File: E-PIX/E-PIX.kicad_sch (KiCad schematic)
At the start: 45 parts, among them J1 USB_C_Receptacle_USB2.0, J2 BNO055, J3 ADC, J4 ADC, Q1 BSS138, Q2 BSS138, SW1 SW, SW2 SW_Push, U1 Conn_03x04, U2 Conn_03x04, U3 TC7WH241FK, U4 TC7WH241FK, U5 NJM7805SDL1, U6 AZ1117-3.3, U7 ESP32-C3-WROOM-02, U8 BTS6142D

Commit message: add SD card mod
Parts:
- removed C6: 1u/16V, Capacitor_SMD:C_0603_1608Metric, symbol Device:C_Small
- removed D3: GREEN, LED_SMD:LED_0603_1608Metric, symbol Device:LED_Small
- removed J3, J4: ADC, Connector_PinHeader_2.54mm:PinHeader_1x03_P2.54mm_Vertical, symbol Connector_Generic:Conn_01x03
- removed R11: 510, Resistor_SMD:R_0603_1608Metric, symbol Device:R_Small
- removed R4, R7, R8: 10k, Resistor_SMD:R_0603_1608Metric, symbol Device:R_Small
- removed SW1: SW, Connector_PinHeader_2.54mm:PinHeader_1x02_P2.54mm_Vertical, symbol Switch:SW_DPST_x2
- removed U7: ESP32-C3-WROOM-02, Espressif:ESP32-C3-WROOM-02, symbol Espressif:ESP32-C3-WROOM-02
- removed U9: ~, IMU:BNO055, symbol IMU:BNO055
- added C6, C9: 47p, symbol Device:C
- added D4: WS2812B, LED_SMD:LED_WS2812B_PLCC4_5.0x5.0mm_P3.2mm, symbol LED:WS2812B
- added Q3, Q4: 2SC4213, Package_TO_SOT_SMD:SOT-323_SC-70, symbol Transistor_BJT:2SC4213
- added R11, R8: 47k, symbol Device:R
- added R15, R16: 470k, symbol Device:R
- added R4, R7: 27, symbol Device:R
- added U10: ESP32-S3-WROOM-1, RF_Module:ESP32-S3-WROOM-1, symbol RF_Module:ESP32-S3-WROOM-1
- added U7: FT231XS, Package_SO:SSOP-20_3.9x8.7mm_P0.635mm, symbol Interface_USB:FT231XS
- C8: value 0.1u/25V -> 0.2u/25V
- J2: footprint Connector_PinHeader_2.54mm:PinHeader_1x05_P2.54mm_Vertical -> Connector_JST:JST_XH_B4B-XH-A_1x04_P2.50mm_Vertical
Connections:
- net ADC1 is gone; now on net +3V3: R1.2
- net +3V3: now also U10.2 (3V3), U7.13 (3V3OUT), U7.3 (VCCIO); no longer C5.1
- net +5V: now also U7.15 (VCC); no longer C2.2
- net BNO055RST: now also U10.18 (IO10)
- net D+: now also R7.2
- net D-: now also R4.1
- net EN1: now also U10.4 (IO4)
- net EN2: now also U10.5 (IO5)
- net GND: now also J1.S1 (SHIELD), C6.1, C9.1, R15.1, R16.1, U10.1 (GND), U10.40 (GND), U10.41 (GND), U7.16 (GND), U7.6 (GND); no longer C2.1, C5.2, R1.1
- net RX1: now also U10.11 (IO18)
- net RX2: now also U10.22 (IO14)
- net SCL: now also U10.17 (IO9)
- net SDA: now also U10.12 (IO8)
- net TX1: now also U10.10 (IO17)
- net TX2: now also U10.21 (IO13)
- net at R9.1: now also U8.2 (IN)
- net at R9.2: no longer U8.2 (IN)
- net RST renamed EN
- net EN: now also R1.1, Q3.3 (C), U10.3 (EN)
- new net: C9.2, R7.1, U7.11 (USBDP)
- new net: Q3.1 (B), R8.1
- new net: C6.2, R4.2, U7.12 (USBDM)
- new net: Q4.1 (B), R11.1
- new net BOOT: Q4.3 (C), U10.27 (IO0)
- new net DTR: Q4.2 (E), R16.2, R8.2, U7.1 (~{DTR})
- new net RTS: Q3.2 (E), R11.2, R15.2, U7.2 (~{RTS})
- new net RX0: U10.36 (RXD0), U7.20 (TXD)
- new net TX0: U10.37 (TXD0), U7.4 (RXD)
- no-connect marks 5 -> 13
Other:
- note added: "Auto boot / Reset"
- note added: "DCDC 7.4V → 3.3V 1.35A"
- note added: "Protection"
- note added: "USB port"
- note added: "USB-Serial convertion"
- note removed: "BNO055"
- note removed: "CPU"
- note removed: "DCDC 5V → 3.3V 1.35A"
- note removed: "Load Switch"
- note removed: "Power supply 5V"
- note removed: "逆流防止用SBD 電圧降下のため デバックにしか使わない"
- moved on the sheet: C1, C2, C3, C4, C5, C7, C8, D1, D2, H1, H2, J1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

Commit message: complete main function. start checking
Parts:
- removed J2: BNO055, Connector_JST:JST_XH_B4B-XH-A_1x04_P2.50mm_Vertical, symbol Connector_Generic:Conn_01x05
- added D3: LED, symbol Device:LED
- added J3: DM3AT-SF-PEJM5, Connector_Card:microSD_HC_Hirose_DM3AT-SF-PEJM5, symbol DM3AT-SF-PEJM5:DM3AT-SF-PEJM5
- added R14: 100, symbol Device:R
- added U9: ~, IMU:BNO055, symbol IMU:BNO055
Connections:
- net +3V3: now also C3.2, C7.2, D4.1 (VDD), D3.2 (A), J3.4 (VDD), U9.1 (VIN); no longer C3.1, C7.1
- net BNO055RST: now also U10.7 (IO7), U9.5 (RESET); no longer U10.18 (IO10)
- net GND: now also C3.1, C7.1, D4.3 (VSS), J3.6 (VSS), J3.P1 (SHIELD), J3.P2 (SHIELD), J3.P3 (SHIELD), J3.P4 (SHIELD), R14.2, U9.2 (GND), U9.7 (GND); no longer C3.2, C7.2
- net RX2: now also U10.14 (IO20); no longer U10.22 (IO14)
- net SCL: now also U9.4 (SCL/R)
- net SDA: now also U9.3 (SDA/T)
- net TX2: now also U10.13 (IO19); no longer U10.21 (IO13)
- net MOSI: now reaches U10.19 (IO11)
- net MOSI: now also J3.3 (CMD)
- net CLK: now reaches U10.20 (IO12)
- net CLK: now also J3.5 (CLK)
- net RGB_led: now reaches U10.25 (IO48)
- net RGB_led: now also D4.4 (DIN)
- new net: D3.1 (K), R14.1
- new net CS: J3.2 (CD/DAT3), U10.18 (IO10)
- new net MISO: J3.7 (DAT0), U10.21 (IO13)
- no-connect marks 13 -> 17
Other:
- note added: "IO"
- note added: "SD card reader"
- note removed: "Output"
- moved on the sheet: C3, C7, D4, H3, H4, Q1, Q2, R12, R13, R5, R6, U1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

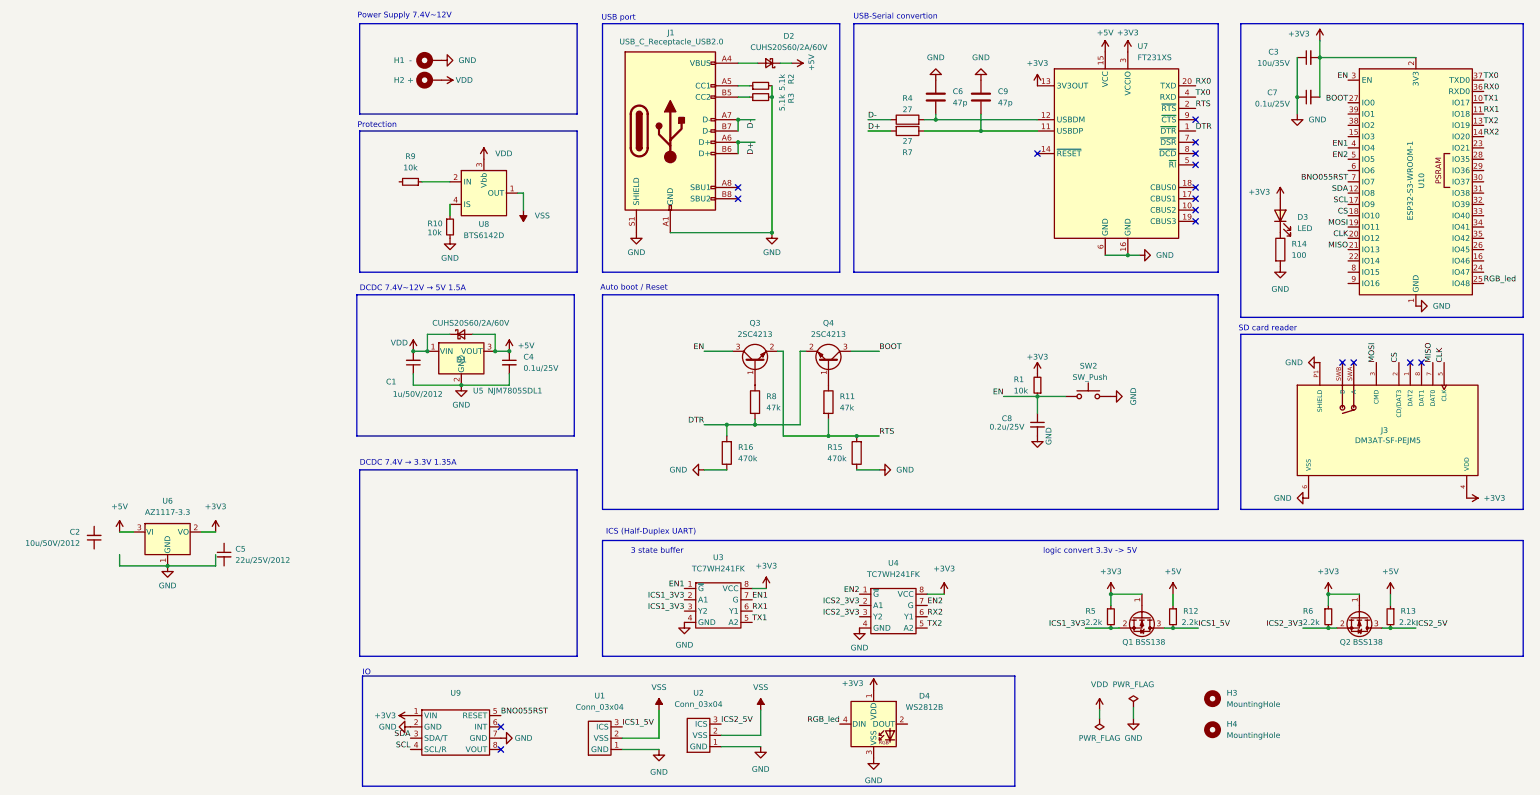
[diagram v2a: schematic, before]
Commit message: finish eeschema. anotate numbers in next step
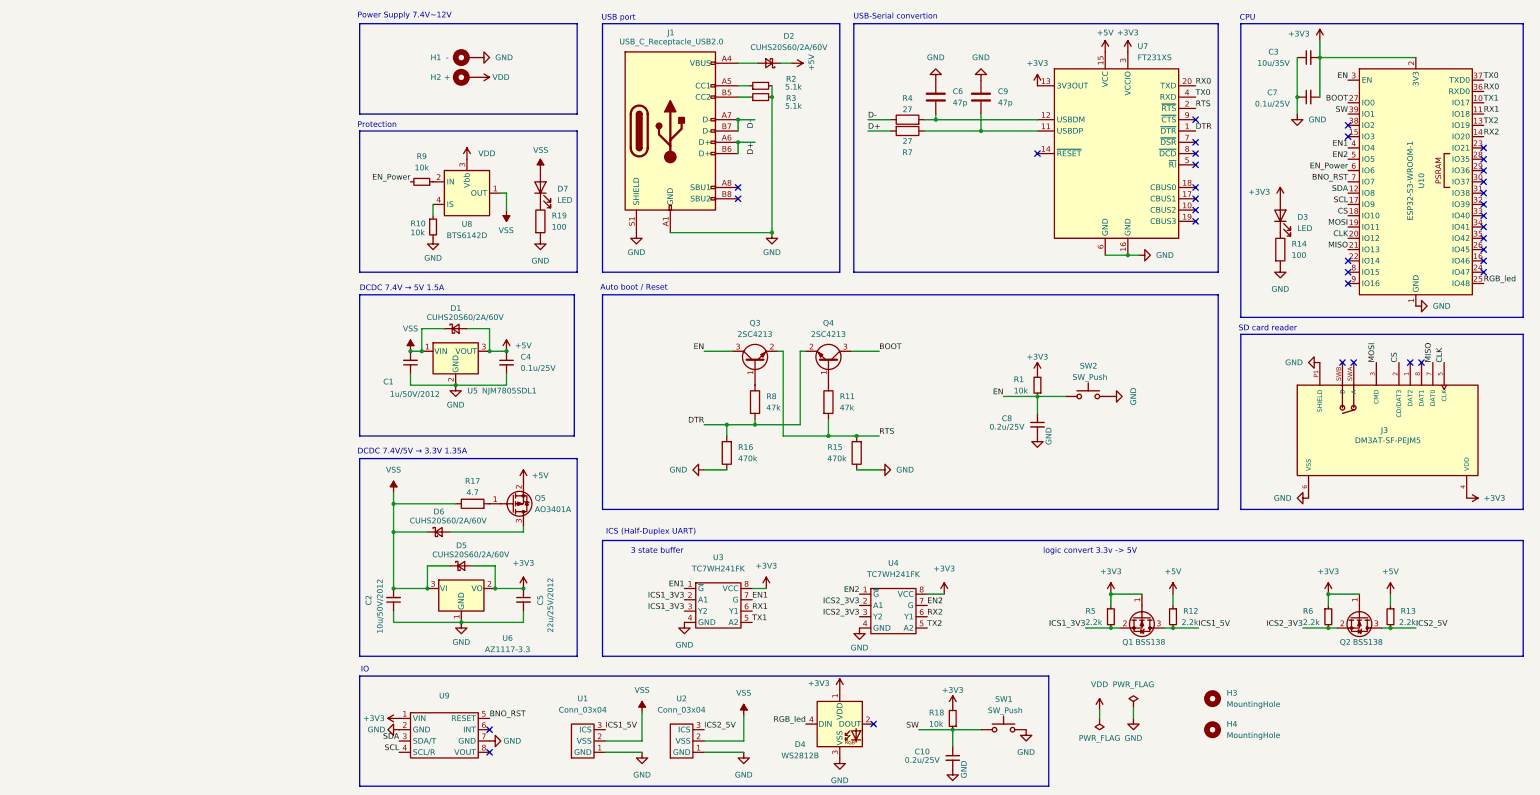
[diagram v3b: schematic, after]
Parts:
- added C10: 0.2u/25V, Capacitor_SMD:C_0603_1608Metric, symbol Device:C_Small
- added D5, D6: CUHS20S60/2A/60V, Diode:Diode_US2H, symbol Device:D_Schottky_Small
- added D7: LED, symbol Device:LED
- added Q5: AO3401A, Package_TO_SOT_SMD:SOT-23, symbol Transistor_FET:AO3401A
- added R17: 4.7, symbol Device:R
- added R18: 10k, Resistor_SMD:R_0603_1608Metric, symbol Device:R_Small
- added R19: 100, symbol Device:R
- added SW1: SW_Push, Button_Switch_SMD:SKRPACE010, symbol Switch:SW_Push
- J3: footprint Connector_Card:microSD_HC_Hirose_DM3AT-SF-PEJM5 -> DM3AT-SF-PEJM5:HRS_DM3AT-SF-PEJM5
- SW2: footprint Button_Switch_SMD:SW_Push_1P1T_NO_Vertical_Wuerth_434133025816 -> Button_Switch_SMD:SKRPACE010
- U5: footprint Package_TO_SOT_SMD:TO-252-2 -> Package_TO_SOT_SMD:SOT-89-3
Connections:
- net +3V3: now also C5.1, D5.2 (A), R18.2
- net +5V: now also Q5.2 (S); no longer U6.3 (VI)
- net GND: now also C2.1, C5.2, C10.2, R19.2, SW1.2
- net VDD: no longer C1.2, D1.1 (K), U5.1 (VIN)
- net VSS: now also C1.2, C2.2, D1.1 (K), U5.1 (VIN), U6.3 (VI), D5.1 (K), D6.1 (K), D7.2 (A), R17.1
- net EN_Power: now reaches R9.2
- net EN_Power: now also U10.6 (IO6)
- net SW: now reaches U10.39 (IO1)
- net SW: now also C10.1, R18.1, SW1.1
- net BNO055RST renamed BNO_RST
- new net: D7.1 (K), R19.1
- new net: D6.2 (A), Q5.3 (D)
- new net: Q5.1 (G), R17.2
- no-connect marks 17 -> 35
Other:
- note added: "CPU"
- note added: "DCDC 7.4V → 5V 1.5A"
- note added: "DCDC 7.4V/5V → 3.3V 1.35A"
- note removed: "DCDC 7.4V → 3.3V 1.35A"
- note removed: "DCDC 7.4V~12V → 5V 1.5A"
- moved on the sheet: C1, C2, C4, C5, D1, D4, H1, H2, R10, R9, U1, U2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

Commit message: finish eeschema. start placing tips
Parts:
- added C2: C_Polarized, Capacitor_THT:CP_Radial_D8.0mm_P3.50mm, symbol Device:C_Polarized
- added C9: 0.1u/25V, Capacitor_SMD:C_0603_1608Metric, symbol Device:C_Small
- added D7: LED, LED_SMD:LED_0603_1608Metric, symbol Device:LED
- added R20: 100, Resistor_SMD:R_0603_1608Metric, symbol Device:R
- C1: renamed from C3; footprint Capacitor_SMD:C_0603_1608Metric -> Capacitor_SMD:C_1206_3216Metric
- C12: renamed from C10; value 0.2u/25V -> 0.1u/25V
- C3: renamed from C6; footprint (none) -> Capacitor_SMD:C_0201_0603Metric
- C4: renamed from C9; footprint (none) -> Capacitor_SMD:C_0201_0603Metric
- C8: value 0.2u/25V -> 0.1u/25V
- D2: renamed from D7; footprint (none) -> LED_SMD:LED_0603_1608Metric
- D3: footprint (none) -> LED_SMD:LED_0603_1608Metric
- J1: footprint Connector_USB:USB_C_Receptacle_XKB_U262-16XN-4BVC11 -> Connector_USB:USB_C_Receptacle_XKB_U262-16XN-4BVC11_with_model
- J2: renamed from J3; footprint DM3AT-SF-PEJM5:HRS_DM3AT-SF-PEJM5 -> Connector_Card:microSD_HC_Hirose_DM3AT-SF-PEJM5
- R10: renamed from R8; footprint (none) -> Resistor_SMD:R_0603_1608Metric
- R11: footprint (none) -> Resistor_SMD:R_0603_1608Metric
- R12: renamed from R16; footprint (none) -> Resistor_SMD:R_0603_1608Metric
- R13: renamed from R15; footprint (none) -> Resistor_SMD:R_0603_1608Metric
- R14: renamed from R17; footprint (none) -> Resistor_SMD:R_0603_1608Metric
- R3: renamed from R4; footprint (none) -> Resistor_SMD:R_0603_1608Metric
- R4: renamed from R7; footprint (none) -> Resistor_SMD:R_0603_1608Metric
- R6: renamed from R19; footprint (none) -> Resistor_SMD:R_0603_1608Metric
- R8: renamed from R14; footprint (none) -> Resistor_SMD:R_0603_1608Metric
- U2: renamed from U10; footprint RF_Module:ESP32-S3-WROOM-1 -> Espressif:ESP32-S3-WROOM-1
- U4: renamed from U5; footprint Package_TO_SOT_SMD:SOT-89-3 -> Package_TO_SOT_SMD:TO-252-2
- U9: renamed from U1; value Conn_03x04 -> Conn_03x02; footprint Conn:PinHeader_03x04_P2.54mm_Vertical -> Conn:PinHeader_03x02_P2.54mm_Vertical
- renumbered C2 to C10, C5 to C11, C7 to C5, C1 to C6, C4 to C7, D2 to D1, D1 to D4, D6 to D5, D5 to D6, D4 to D8, Q3 to Q1, Q4 to Q2, Q5 to Q3, Q1 to Q4, Q2 to Q5, R2 to R1, R5 to R15, R12 to R16, R6 to R17, R13 to R18, R18 to R19, R3 to R2, R9 to R5, R10 to R7, R1 to R9, SW2 to SW1, SW1 to SW2, U7 to U1, U2 to U10, U8 to U3, U3 to U5, U4 to U6, U6 to U7, U9 to U8
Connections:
- net EN: now also C9.1
- net GND: now also C2.2, C9.2, R20.2
- net VDD: now also C2.1
- net led: now reaches U2.24 (IO47)
- net led: now also D7.2 (A)
- new net: D7.1 (K), R20.1
- no-connect marks 35 -> 34
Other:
- moved on the sheet: C12, D8, H1, H2, R19, SW2, U10, U9

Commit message: update some pin mappings of ESP
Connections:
- net EN1: now also U2.22 (IO14); no longer U2.4 (IO4)
- net EN2: now also U2.23 (IO21); no longer U2.5 (IO5)
- net EN_Power: now also U2.26 (IO45); no longer U2.6 (IO6)
- net SW: now also U2.28 (IO35); no longer U2.39 (IO1)
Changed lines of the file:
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@@
-	)
-	(no_connect
-		(at 271.78 46.99)
 	)
 	(no_connect
@@
 	)
 	(no_connect
-		(at 271.78 69.85)
-	)
-	(no_connect
 		(at 271.78 62.23)
 	)
@@
 	)
 	(no_connect
+		(at 241.3 52.07)
+	)
+	(no_connect
+		(at 241.3 49.53)
+	)
+	(no_connect
 		(at 271.78 59.69)
 	)
@@
 	)
 	(no_connect
+		(at 241.3 39.37)
+	)
+	(no_connect
 		(at 271.78 72.39)
 	)
@@
 	)
 	(no_connect
+		(at 241.3 46.99)
+	)
+	(no_connect
 		(at 207.01 58.42)
 	)
@@
 	)
 	(no_connect
-		(at 241.3 72.39)
-	)
-	(no_connect
 		(at 171.45 48.26)
 	)
@@
 	(no_connect
 		(at 241.3 74.93)
-	)
-	(no_connect
-		(at 271.78 49.53)
 	)
 	(no_connect
@@
 	)
 	(label "EN1"
-		(at 241.3 46.99 180)
+		(at 241.3 72.39 180)
 		(effects
 			(font
@@
 	)
 	(label "EN_Power"
-		(at 241.3 52.07 180)
-		(effects
-			(font
-				(size 1.27 1.27)
-			)
-			(justify right bottom)
+		(at 271.78 69.85 0)
+		(effects
+			(font
+				(size 1.27 1.27)
+			)
+			(justify left bottom)
 		)
 	)
@@
 	)
 	(label "EN2"
-		(at 241.3 49.53 180)
-		(effects
-			(font
-				(size 1.27 1.27)
-			)
-			(justify right bottom)
+		(at 271.78 46.99 0)
+		(effects
+			(font
+				(size 1.27 1.27)
+			)
+			(justify left bottom)
 		)
 	)
@@
 	)
 	(label "SW"
-		(at 241.3 39.37 180)
-		(effects
-			(font
-				(size 1.27 1.27)
-			)
-			(justify right bottom)
-		)
-	)
+		(at 271.78 49.53 0)
+		(effects
+			(font
+				(size 1.27 1.27)
+			)
+			(justify left bottom)
+		)
+	)

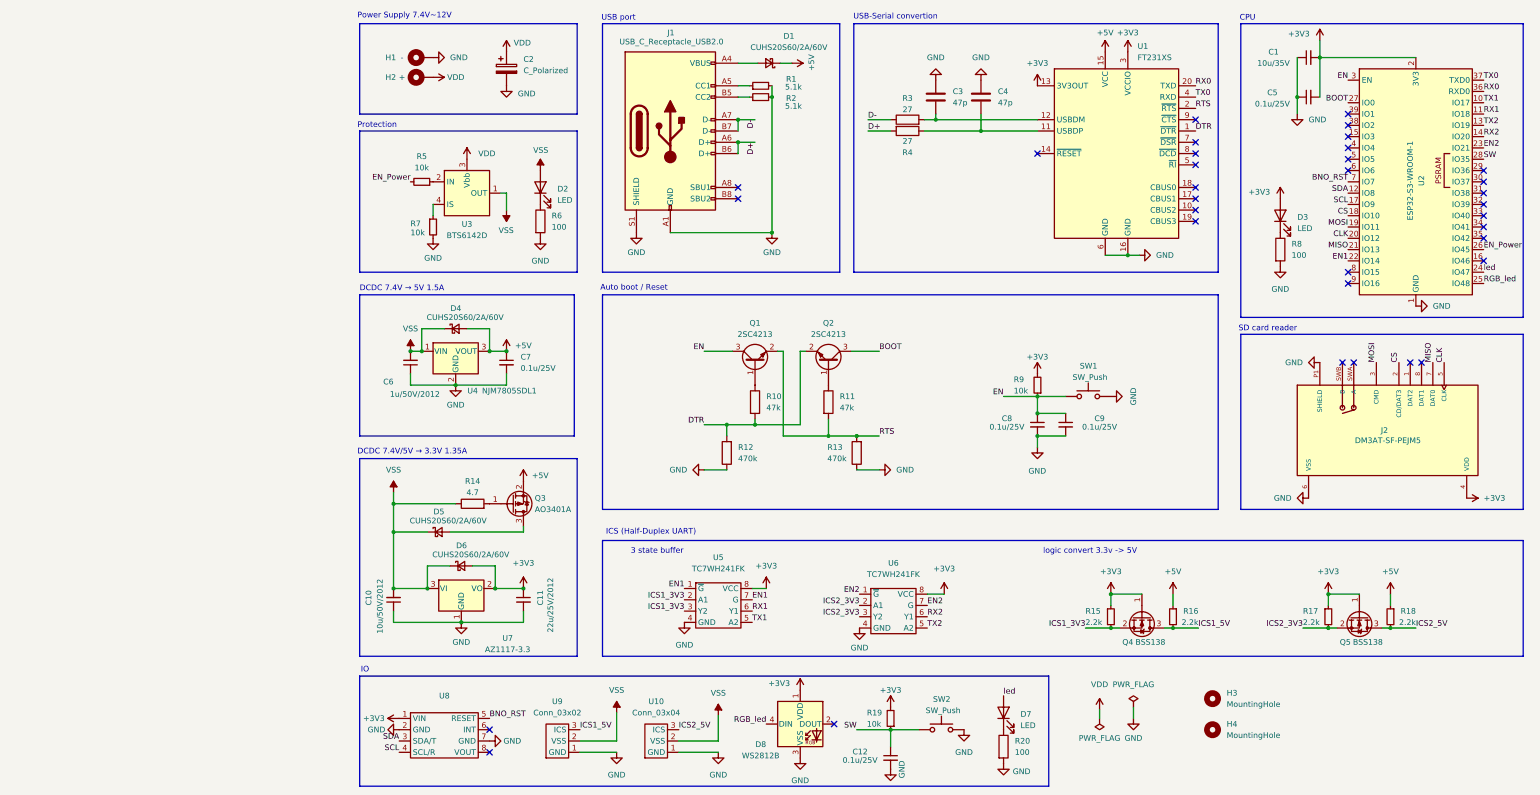
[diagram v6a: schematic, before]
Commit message: place all the tips
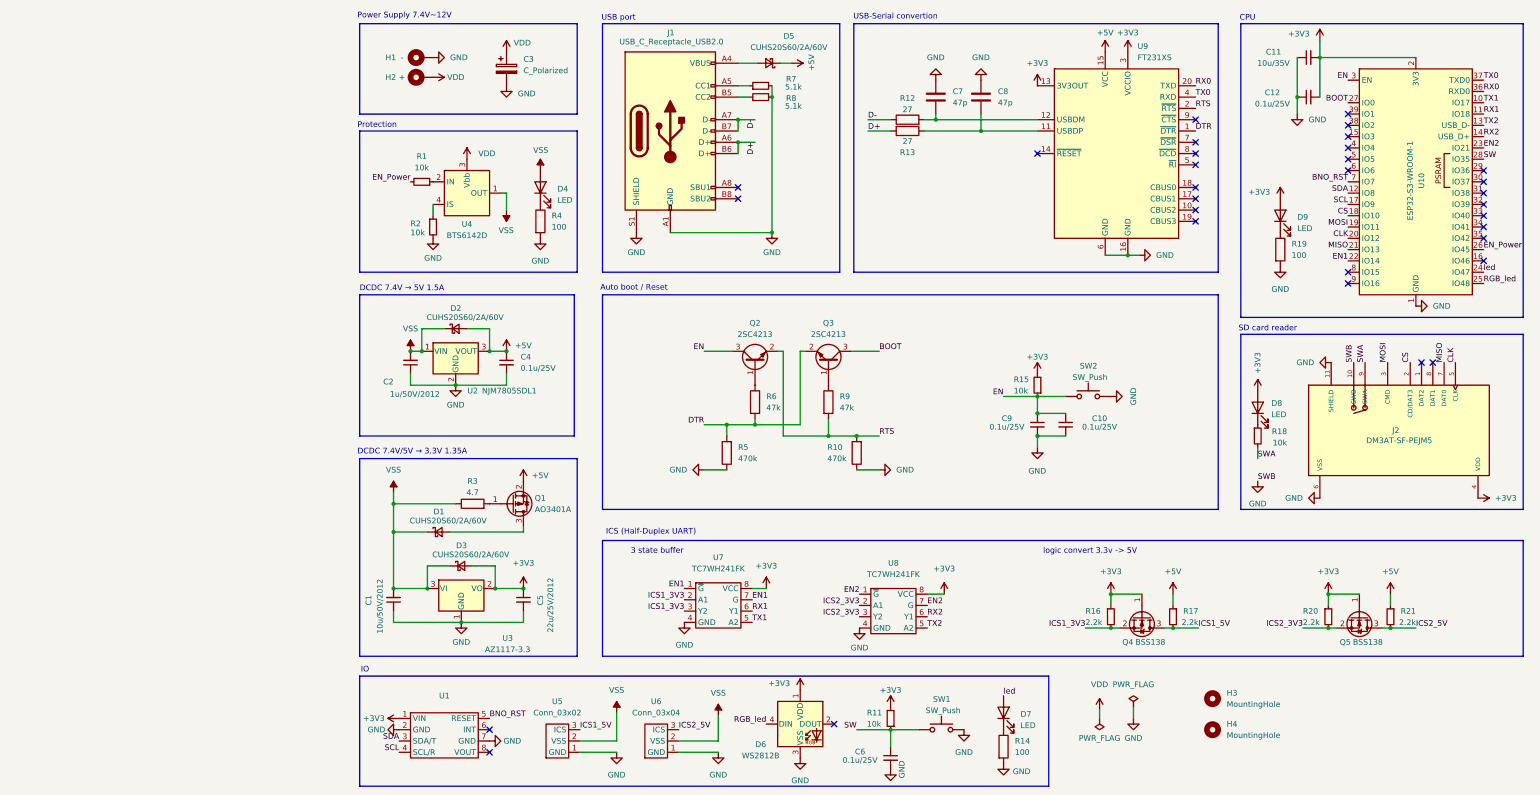
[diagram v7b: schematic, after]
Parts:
- added D8: LED, LED_SMD:LED_0603_1608Metric, symbol Device:LED
- added R18: 10k, Resistor_SMD:R_0603_1608Metric, symbol Device:R_Small
- J2: Description_1 10 (8 + 2) Position Card Connector Secure Digital - microSD™ Surface Mount, Right Angle Gold -> 10 (8 + 2) Position Card Connector Secure Digital - microSD™ Surface Mount, Right Angle Gold
- renumbered C10 to C1, C9 to C10, C1 to C11, C5 to C12, C6 to C2, C2 to C3, C7 to C4, C11 to C5, C12 to C6, C3 to C7, C4 to C8, C8 to C9, D5 to D1, D4 to D2, D6 to D3, D2 to D4, D1 to D5, D8 to D6, D3 to D9, Q3 to Q1, Q1 to Q2, Q2 to Q3, R5 to R1, R13 to R10, R19 to R11, R3 to R12, R4 to R13, R20 to R14, R9 to R15, R15 to R16, R16 to R17, R8 to R19, R7 to R2, R17 to R20, R18 to R21, R14 to R3, R6 to R4, R12 to R5, R10 to R6, R1 to R7, R2 to R8, R11 to R9, SW2 to SW1, SW1 to SW2, U8 to U1, U2 to U10, U4 to U2, U7 to U3, U3 to U4, U9 to U5, U10 to U6, U5 to U7, U6 to U8, U1 to U9
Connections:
- net +3V3: now also D8.2 (A)
- net GND: now also J2.10 (SWB), J2.11 (SHIELD); no longer J2.P1 (SHIELD), J2.P2 (SHIELD), J2.P3 (SHIELD), J2.P4 (SHIELD)
- new net: D8.1 (K), R18.1
- new net SWA: J2.9 (SWA), R18.2
- no-connect marks 34 -> 32
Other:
- moved on the sheet: J2

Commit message: move some tips
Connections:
- net EN1: now also U10.9 (IO16); no longer U10.22 (IO14)
- net EN2: now also U10.15 (IO3); no longer U10.23 (IO21)
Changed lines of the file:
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@@
+	)
+	(no_connect
+		(at 241.3 74.93)
 	)
 	(no_connect
@@
 	)
 	(no_connect
+		(at 241.3 72.39)
+	)
+	(no_connect
 		(at 271.78 54.61)
-	)
-	(no_connect
-		(at 241.3 74.93)
 	)
 	(no_connect
@@
 	)
 	(no_connect
+		(at 271.78 46.99)
+	)
+	(no_connect
 		(at 207.01 48.26)
-	)
-	(no_connect
-		(at 241.3 44.45)
 	)
 	(no_connect
@@
 	)
 	(no_connect
-		(at 241.3 77.47)
-	)
-	(no_connect
 		(at 207.01 45.72)
 	)
@@
 	)
 	(label "EN1"
-		(at 241.3 72.39 180)
+		(at 241.3 77.47 180)
 		(effects
 			(font
@@
 	)
 	(label "EN2"
-		(at 271.78 46.99 0)
-		(effects
-			(font
-				(size 1.27 1.27)
-			)
-			(justify left bottom)
-		)
-	)
+		(at 241.3 44.45 180)
+		(effects
+			(font
+				(size 1.27 1.27)
+			)
+			(justify right bottom)
+		)
+	)
